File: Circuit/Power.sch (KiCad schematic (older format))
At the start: 16 parts, among them Q201 FDN340P, Q202 FDN340P, Q203 FDN340P, U201 CN3063, U202 MCP6002

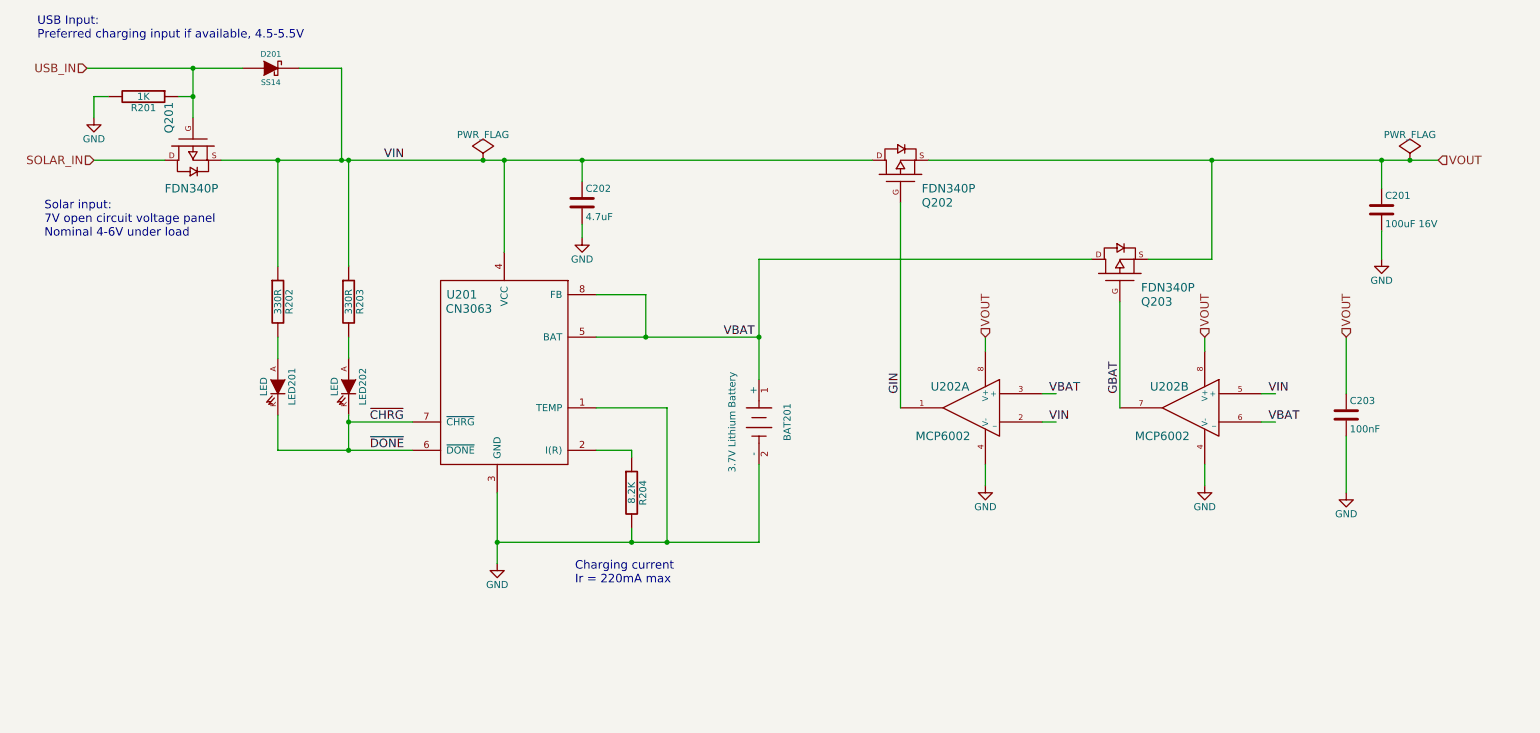
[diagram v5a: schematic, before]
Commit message: Flesh out schematic sensor elements, etc.
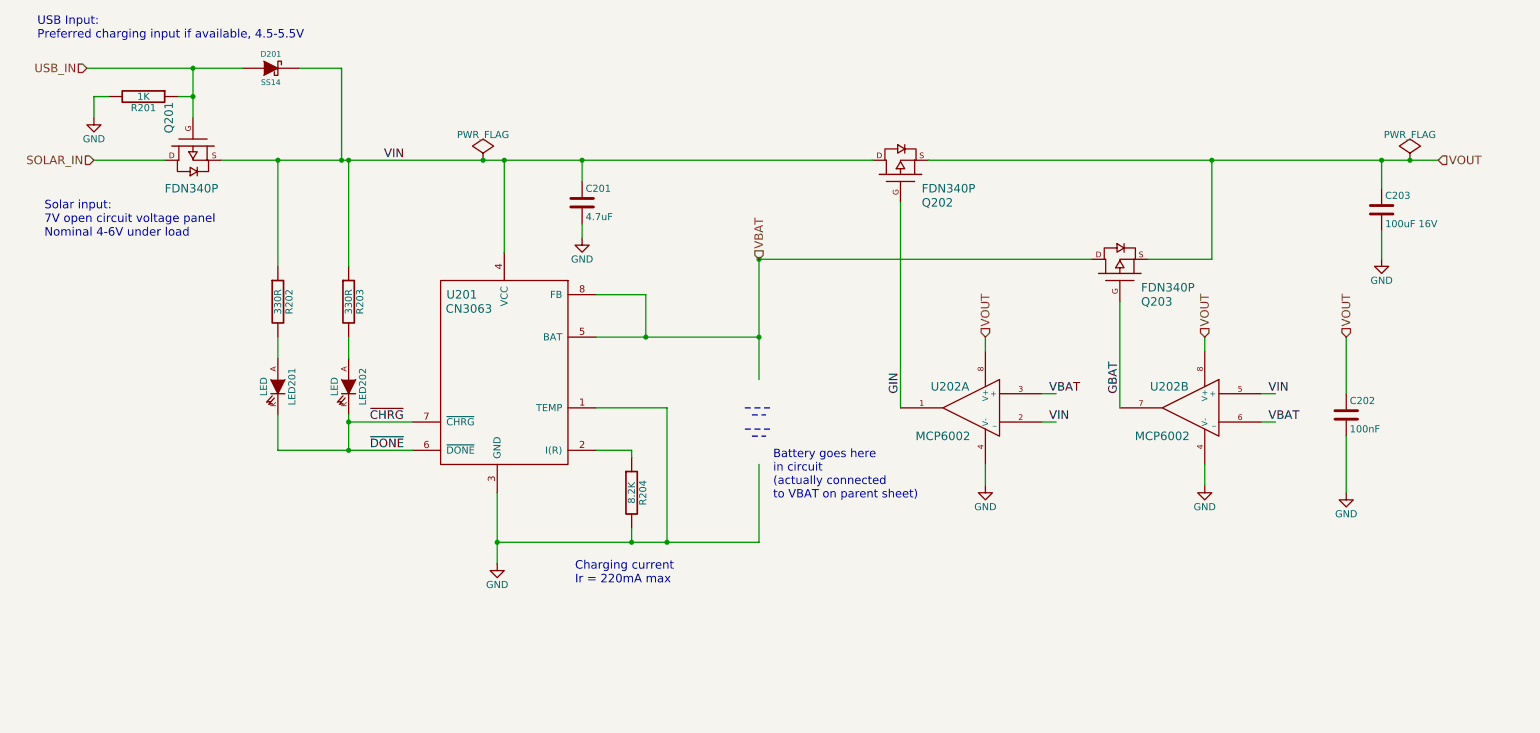
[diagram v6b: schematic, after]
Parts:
- removed BAT201: 3.7V Lithium Battery, symbol BATTERY
- renumbered C202 to C201, C203 to C202, C201 to C203
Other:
- note added: "Battery goes here\nin circuit\n(actually connected\nto VBAT on parent sheet)"
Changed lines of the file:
@@
 $Descr A4 11693 8268
 encoding utf-8
-Sheet 2 2
+Sheet 2 4
 Title ""
 Date ""
@@
 SOLAR_IN
 $Comp
-L BATTERY BAT201
-U 1 1 563C4CDD
-P 5850 3650
-F 0 "BAT201" H 5850 3850 50  0000 C CNN
-F 1 "3.7V Lithium Battery" H 5850 3460 50  0000 C CNN
-F 2 "" H 5850 3650 60  0000 C CNN
-F 3 "" H 5850 3650 60  0000 C CNN
-	1    5850 3650
-	0    1    1    0
-$EndComp
-$Comp
-L GND #PWR202
+L GND #PWR023
 U 1 1 563C4E24
 P 4000 4650
-F 0 "#PWR202" H 4000 4400 50  0001 C CNN
+F 0 "#PWR023" H 4000 4400 50  0001 C CNN
 F 1 "GND" H 4000 4500 50  0000 C CNN
 F 2 "" H 4000 4650 60  0000 C CNN
@@
 $EndComp
 $Comp
-L GND #PWR201
+L GND #PWR024
 U 1 1 563C5B2C
 P 1150 1500
-F 0 "#PWR201" H 1150 1250 50  0001 C CNN
+F 0 "#PWR024" H 1150 1250 50  0001 C CNN
 F 1 "GND" H 1150 1350 50  0000 C CNN
 F 2 "" H 1150 1500 60  0000 C CNN
@@
 Text Label 3100 3850 0    60   ~ 0
 ~DONE
-Wire Wire Line
-	5050 3050 5050 2750
-Wire Wire Line
-	5050 2750 4700 2750
-Connection ~ 5050 3050
-Wire Wire Line
-	4700 3550 5200 3550
-Wire Wire Line
-	5200 4500 5200 3550
-Wire Wire Line
-	4000 4150 4000 4650
-Wire Wire Line
-	4950 3900 4950 3850
-Wire Wire Line
-	4950 3850 4700 3850
-Wire Wire Line
-	4050 1800 4050 2450
-Connection ~ 4050 1800
-Wire Wire Line
-	1150 1800 1650 1800
-Wire Wire Line
-	1850 1150 1850 1500
-Wire Wire Line
-	1100 1150 2200 1150
-Connection ~ 1850 1150
-Wire Wire Line
-	2600 1150 2900 1150
-Wire Wire Line
-	2900 1800 2900 1150
-Connection ~ 2900 1800
-Wire Wire Line
-	1750 1350 1850 1350
-Connection ~ 1850 1350
-Wire Wire Line
-	1150 1350 1250 1350
-Wire Wire Line
-	1150 1350 1150 1500
-Wire Wire Line
-	2050 1800 6650 1800
-Wire Wire Line
-	2950 3650 3400 3650
-Wire Wire Line
-	2950 2550 2950 1800
-Connection ~ 2950 1800
-Wire Wire Line
-	2950 3600 2950 3850
-Connection ~ 2950 3650
-Wire Wire Line
-	2950 3050 2950 3200
-Connection ~ 2950 3850
-Wire Wire Line
-	6850 2100 6850 3550
-Wire Wire Line
-	2450 3850 3400 3850
-Wire Wire Line
-	2450 3050 2450 3200
-Wire Wire Line
-	2450 2550 2450 1800
-Connection ~ 2450 1800
-Wire Wire Line
-	2450 3600 2450 3850
 $Comp
 L MOSFET_P Q202
@@
 Text Notes 4550 4800 0    60   ~ 0
 Charging current\nIr = 220mA max
-Wire Wire Line
-	4000 4500 5850 4500
-Connection ~ 4000 4500
-Wire Wire Line
-	4950 4400 4950 4500
-Connection ~ 4950 4500
-Connection ~ 5200 4500
-$Comp
-L GND #PWR204
+$Comp
+L GND #PWR025
 U 1 1 56417FB3
 P 7450 4100
-F 0 "#PWR204" H 7450 3850 50  0001 C CNN
+F 0 "#PWR025" H 7450 3850 50  0001 C CNN
 F 1 "GND" H 7450 3950 50  0000 C CNN
 F 2 "" H 7450 4100 60  0000 C CNN
@@
 	0    -1   -1   0
 $EndComp
-Wire Wire Line
-	4700 3050 5850 3050
-Connection ~ 5850 3050
-Wire Wire Line
-	5850 2500 5850 3350
-Wire Wire Line
-	5850 2500 8200 2500
-Wire Wire Line
-	8400 2800 8400 3550
-Text Label 5600 3050 0    60   ~ 0
-VBAT
-Connection ~ 9050 1800
-Wire Wire Line
-	8600 2500 9050 2500
 Text Label 8400 3450 1    60   ~ 0
 GBAT
 Text Label 6850 3450 1    60   ~ 0
 GIN
-Wire Wire Line
-	7050 1800 10650 1800
-Wire Wire Line
-	10250 1800 10250 2000
 Text HLabel 10650 1800 2    60   Input ~ 0
 VOUT
-Connection ~ 10250 1800
-Wire Wire Line
-	10250 2300 10250 2500
-$Comp
-L GND #PWR207
+$Comp
+L GND #PWR026
 U 1 1 5641AA9F
 P 10250 2500
-F 0 "#PWR207" H 10250 2250 50  0001 C CNN
+F 0 "#PWR026" H 10250 2250 50  0001 C CNN
 F 1 "GND" H 10250 2350 50  0000 C CNN
 F 2 "" H 10250 2500 60  0000 C CNN
@@
 	-1   0    0    -1
 $EndComp
-Wire Wire Line
-	7450 4100 7450 3950
-Wire Wire Line
-	9050 2500 9050 1800
-Wire Wire Line
-	7450 3150 7450 3050
 Text HLabel 7450 3050 1    60   Input ~ 0
 VOUT
-Wire Wire Line
-	9000 3150 9000 3050
 Text HLabel 9000 3050 1    60   Input ~ 0
 VOUT
 $Comp
-L GND #PWR205
+L GND #PWR027
 U 1 1 5642C1C1
 P 9000 4100
-F 0 "#PWR205" H 9000 3850 50  0001 C CNN
+F 0 "#PWR027" H 9000 3850 50  0001 C CNN
 F 1 "GND" H 9000 3950 50  0000 C CNN
 F 2 "" H 9000 4100 60  0000 C CNN
@@
 	-1   0    0    -1
 $EndComp
-Wire Wire Line
-	9000 4100 9000 3950
-Wire Wire Line
-	7850 3650 7950 3650
-Wire Wire Line
-	7850 3450 7950 3450
-Wire Wire Line
-	9400 3450 9500 3450
-Wire Wire Line
-	9400 3650 9500 3650
 Text Label 9450 3650 0    60   ~ 0
 VBAT
@@
 VIN
 $Comp
-L C C201
+L C C203
 U 1 1 5642CCBE
 P 10250 2150
-F 0 "C201" H 10275 2250 50  0000 L CNN
+F 0 "C203" H 10275 2250 50  0000 L CNN
 F 1 "100uF 16V" H 10275 2050 50  0000 L CNN
 F 2 "" H 10288 2000 30  0000 C CNN
@@
 	1    0    0    -1
 $EndComp
-Wire Wire Line
-	5850 4500 5850 3950
-$Comp
-L PWR_FLAG #FLG202
+$Comp
+L PWR_FLAG #FLG028
 U 1 1 5642D1CE
 P 10450 1800
-F 0 "#FLG202" H 10450 1895 50  0001 C CNN
+F 0 "#FLG028" H 10450 1895 50  0001 C CNN
 F 1 "PWR_FLAG" H 10450 1980 50  0000 C CNN
 F 2 "" H 10450 1800 60  0000 C CNN
@@
 	1    0    0    -1
 $EndComp
-Connection ~ 10450 1800
-$Comp
-L PWR_FLAG #FLG201
+$Comp
+L PWR_FLAG #FLG029
 U 1 1 5642D5A3
 P 3900 1800
-F 0 "#FLG201" H 3900 1895 50  0001 C CNN
+F 0 "#FLG029" H 3900 1895 50  0001 C CNN
 F 1 "PWR_FLAG" H 3900 1980 50  0000 C CNN
 F 2 "" H 3900 1800 60  0000 C CNN
@@
 	1    0    0    -1
 $EndComp
-Connection ~ 3900 1800
-$Comp
-L C C203
+$Comp
+L C C202
 U 1 1 5642D8F0
 P 10000 3600
-F 0 "C203" H 10025 3700 50  0000 L CNN
+F 0 "C202" H 10025 3700 50  0000 L CNN
 F 1 "100nF" H 10025 3500 50  0000 L CNN
 F 2 "" H 10038 3450 30  0000 C CNN
@@
 	1    0    0    -1
 $EndComp
-Wire Wire Line
-	10000 3450 10000 3050
-Wire Wire Line
-	10000 3750 10000 4150
-$Comp
-L GND #PWR206
+$Comp
+L GND #PWR030
 U 1 1 5642DA26
 P 10000 4150
-F 0 "#PWR206" H 10000 3900 50  0001 C CNN
+F 0 "#PWR030" H 10000 3900 50  0001 C CNN
 F 1 "GND" H 10000 4000 50  0000 C CNN
 F 2 "" H 10000 4150 60  0000 C CNN
@@
 VOUT
 $Comp
-L C C202
+L C C201
 U 1 1 5642CCB8
 P 4600 2100
-F 0 "C202" H 4625 2200 50  0000 L CNN
+F 0 "C201" H 4625 2200 50  0000 L CNN
 F 1 "4.7uF" H 4625 2000 50  0000 L CNN
 F 2 "" H 4638 1950 30  0000 C CNN
@@
 	1    0    0    -1
 $EndComp
-Wire Wire Line
-	4600 1950 4600 1800
-Connection ~ 4600 1800
-Wire Wire Line
-	4600 2250 4600 2350
-$Comp
-L GND #PWR203
+$Comp
+L GND #PWR031
 U 1 1 5642CE9D
 P 4600 2350
-F 0 "#PWR203" H 4600 2100 50  0001 C CNN
+F 0 "#PWR031" H 4600 2100 50  0001 C CNN
 F 1 "GND" H 4600 2200 50  0000 C CNN
 F 2 "" H 4600 2350 60  0000 C CNN
@@
 	1    0    0    -1
 $EndComp
+Text HLabel 5850 2500 1    60   Input ~ 0
+VBAT
+Wire Wire Line
+	5050 3050 5050 2750
+Wire Wire Line
+	5050 2750 4700 2750
+Connection ~ 5050 3050
+Wire Wire Line
+	4700 3550 5200 3550
+Wire Wire Line
+	5200 3550 5200 4500
+Wire Wire Line
+	4000 4150 4000 4650
+Wire Wire Line
+	4950 3900 4950 3850
+Wire Wire Line
+	4950 3850 4700 3850
+Wire Wire Line
+	4050 1800 4050 2450
+Connection ~ 4050 1800
+Wire Wire Line
+	1150 1800 1650 1800
+Wire Wire Line
+	1850 1150 1850 1500
+Wire Wire Line
+	1100 1150 2200 1150
+Connection ~ 1850 1150
+Wire Wire Line
+	2600 1150 2900 1150
+Wire Wire Line
+	2900 1150 2900 1800
+Connection ~ 2900 1800
+Wire Wire Line
+	1750 1350 1850 1350
+Connection ~ 1850 1350
+Wire Wire Line
+	1150 1350 1250 1350
+Wire Wire Line
+	1150 1350 1150 1500
+Wire Wire Line
+	2050 1800 6650 1800
+Wire Wire Line
+	2950 3650 3400 3650
+Wire Wire Line
+	2950 2550 2950 1800
+Connection ~ 2950 1800
+Wire Wire Line
+	2950 3600 2950 3850
+Connection ~ 2950 3650
+Wire Wire Line
+	2950 3050 2950 3200
+Connection ~ 2950 3850
+Wire Wire Line
+	6850 2100 6850 3550
+Wire Wire Line
+	2450 3850 3400 3850
+Wire Wire Line
+	2450 3050 2450 3200
+Wire Wire Line
+	2450 2550 2450 1800
+Connection ~ 2450 1800
+Wire Wire Line
+	2450 3600 2450 3850
+Wire Wire Line
+	4000 4500 5850 4500
+Connection ~ 4000 4500
+Wire Wire Line
+	4950 4400 4950 4500
+Connection ~ 4950 4500
+Connection ~ 5200 4500
+Wire Wire Line
+	4700 3050 5850 3050
+Connection ~ 5850 3050
+Wire Wire Line
+	5850 2500 5850 3350
+Wire Wire Line
+	5850 2500 8200 2500
+Wire Wire Line
+	8400 2800 8400 3550
+Connection ~ 9050 1800
+Wire Wire Line
+	8600 2500 9050 2500
+Wire Wire Line
+	7050 1800 10650 1800
+Wire Wire Line
+	10250 1800 10250 2000
+Connection ~ 10250 1800
+Wire Wire Line
+	10250 2300 10250 2500
+Wire Wire Line
+	7450 4100 7450 3950
+Wire Wire Line
+	9050 2500 9050 1800
+Wire Wire Line
+	7450 3150 7450 3050
+Wire Wire Line
+	9000 3150 9000 3050
+Wire Wire Line
+	9000 4100 9000 3950
+Wire Wire Line
+	7850 3650 7950 3650
+Wire Wire Line
+	7850 3450 7950 3450
+Wire Wire Line
+	9400 3450 9500 3450
+Wire Wire Line
+	9400 3650 9500 3650
+Wire Wire Line
+	5850 4500 5850 3950
+Connection ~ 10450 1800
+Connection ~ 3900 1800
+Wire Wire Line
+	10000 3450 10000 3050
+Wire Wire Line
+	10000 3750 10000 4150
+Wire Wire Line
+	4600 1950 4600 1800
+Connection ~ 4600 1800
+Wire Wire Line
+	4600 2250 4600 2350
+Connection ~ 5850 2500
+Wire Notes Line
+	5750 3550 5950 3550
+Wire Notes Line
+	5800 3600 5900 3600
+Wire Notes Line
+	5750 3700 5950 3700
+Wire Notes Line
+	5800 3750 5900 3750
+Text Notes 5950 4200 0    59   ~ 0
+Battery goes here\nin circuit\n(actually connected\nto VBAT on parent sheet)
 $EndSCHEMATC
